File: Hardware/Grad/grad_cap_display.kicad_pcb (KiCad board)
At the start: 4 copper layers, 76.5 x 76.5 mm, 62 parts, among them J101 6-Pos 2.54mm Header, J1101 JST-PH SPI, J1102 JST-PH UART/I2C, J1103 JST-PH A#, J1104 Micro_SD_Card, J201 Amphenol 40-Pin FPC, J202 01x30 Pads, J203 01x30 Pads, J204 01x30 Pads, J205 01x30 Pads, J3 2x8 2.54mm IDC Header, U1101 TC7MBL3126CFT, U1102 AZ1117-5.0, U1103 THVD1400D, U1104 QTPy SAMD21, U201 LM66200DRLR, U202 TLV75733PDRV, U203 SN74LVC1G139, U204 ESP32-S3-WROOM-1-N8R8, U205 TC7MBL3126CFT, U206 AP3019AKTTR, U207 W25Q128JVP, U208 THVD1400D

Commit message: More routing progress
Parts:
- removed C1101, C1104, C1105: 100nF, Capacitor_SMD:C_0402_1005Metric
- removed C1102, C1103, C1106: 22uF, Capacitor_SMD:C_0603_1608Metric
- removed C201, C203: 1uF, New_Library:Worthington_C_0603
- removed C202, C204, C206, C215: 22uF, New_Library:Worthington_C_0603
- removed C205, C207, C208, C209, C210, C211, C213, C214, C216: 100nF, New_Library:Worthington_C_0402
- removed C212: 22uF, New_Library:Worthington_D_0603
- removed D1101, D1102: LED_Small, New_Library:Worthington_LED_0603
- removed D201, D202, D203, D204, D205: RED, New_Library:Worthington_LED_0603
- removed J1101: JST-PH SPI, Connector_JST:JST_PH_S5B-PH-K_1x05_P2.00mm_Horizontal
- removed J1102: JST-PH UART/I2C, Connector_JST:JST_PH_S6B-PH-K_1x06_P2.00mm_Horizontal
- removed J1103: JST-PH A#, Connector_JST:JST_PH_S6B-PH-K_1x06_P2.00mm_Horizontal
- removed L201: 22uH, New_Library:CDRH5D28
- removed R1101: 1k, New_Library:Worthington_R_0402
- removed R1102, R201: 430, New_Library:Worthington_R_0402
- removed R202: 10, Resistor_SMD:R_1210_3225Metric
- removed R203: 120, New_Library:Worthington_R_0402
- removed RN1101: 47k, New_Library:RESCAXE80P320X160X70-8N
- removed RN201: 10k, New_Library:RESCAXE80P320X160X70-8N
- removed RN202: 430, New_Library:RESCAXE80P320X160X70-8N
- removed U1101, U205: TC7MBL3126CFT, Package_SO:TSSOP-14_4.4x5mm_P0.65mm
- removed U1102: AZ1117-5.0, Package_TO_SOT_SMD:SOT-223-3_TabPin2
- removed U1103, U208: THVD1400D, Package_SO:SOIC-8_3.9x4.9mm_P1.27mm
- removed U201: LM66200DRLR, Package_TO_SOT_SMD:SOT-583-8
- removed U202: TLV75733PDRV, Package_SON:WSON-6-1EP_2x2mm_P0.65mm_EP1x1.6mm
- removed U203: SN74LVC1G139, Package_SO:VSSOP-8_2.3x2mm_P0.5mm
- removed U206: AP3019AKTTR, Package_TO_SOT_SMD:TSOT-23-6
- removed U207: W25Q128JVP, Package_SON:WSON-8-1EP_6x5mm_P1.27mm_EP3.4x4.3mm
- added C101: 22uF, New_Library:Worthington_C_0603, F.Cu at (61.2, 9.75)
- added C102: 22uF, New_Library:Worthington_C_0603, F.Cu at (4.15, 5.95)
- added C103: 22uF, New_Library:Worthington_C_0603, F.Cu at (9.65, 11.8)
- added C104: 22uF, New_Library:Worthington_C_0603, F.Cu at (16.4, 11.7)
- added C105: 100nF, New_Library:Worthington_C_0402, F.Cu at (18.1, 12.0)
- added C106: 100nF, New_Library:Worthington_C_0402, F.Cu at (14.8, 12.0)
- added C107: 22uF, New_Library:Worthington_C_0603, F.Cu at (22.8, 11.6)
- added C108: 100nF, New_Library:Worthington_C_0402, F.Cu at (61.2, 13.1)
- added C109: 100nF, New_Library:Worthington_C_0402, F.Cu at (25.8, 11.2)
- added C110: 100nF, New_Library:Worthington_C_0402, F.Cu at (24.4, 11.2)
- added C111: 100nF, New_Library:Worthington_C_0402, F.Cu at (56.4, 6.85)
- added C112: 100nF, New_Library:Worthington_C_0402, F.Cu at (58.3, 23.0)
- added C113: 22uF, New_Library:Worthington_C_0603, F.Cu at (68.5, 68.7)
- added C114: 100nF, New_Library:Worthington_C_0402, F.Cu at (52.1, 57.0)
- added C115: 100nF, New_Library:Worthington_C_0402, F.Cu at (67.1, 68.4)
- added C116: 22uF, New_Library:Worthington_C_0603, F.Cu at (52.4, 58.5)
- added C217: 100nF, Capacitor_SMD:C_0402_1005Metric, F.Cu at (29.3, 39.7)
- added C218: 22uF, Capacitor_SMD:C_0603_1608Metric, F.Cu at (7.50, 23.8)
- added C219: 22uF, Capacitor_SMD:C_0603_1608Metric, F.Cu at (10.4, 24.6)
- added C220: 100nF, Capacitor_SMD:C_0402_1005Metric, F.Cu at (10.2, 26.0)
- added C221: 100nF, Capacitor_SMD:C_0402_1005Metric, F.Cu at (56.0, 41.5)
- added C222: 22uF, Capacitor_SMD:C_0603_1608Metric, F.Cu at (54.6, 42.0)
- added C223: 22uF, Capacitor_SMD:C_0603_1608Metric, F.Cu at (17.3, 26.4)
- added C401: 100nF, New_Library:Worthington_C_0402, F.Cu at (53.3, 14.2)
- added C402: 100nF, Capacitor_SMD:C_0402_1005Metric, F.Cu at (37.1, 45.0)
- added D101: RED, New_Library:Worthington_LED_0603, F.Cu at (19.6, 11.6)
- added D102: RED, New_Library:Worthington_LED_0603, F.Cu at (47.6, 80.8)
- added D103: RED, New_Library:Worthington_LED_0603, F.Cu at (47.6, 83.3)
- added D104: RED, New_Library:Worthington_LED_0603, F.Cu at (47.6, 85.8)
- added D105: RED, New_Library:Worthington_LED_0603, F.Cu at (47.6, 88.3)
- added D206: RED, New_Library:Worthington_LED_0603, F.Cu at (12.8, 19.8)
- added D207: RED, New_Library:Worthington_LED_0603, F.Cu at (65.4, 47.5)
- added D208: RED, New_Library:Worthington_LED_0603, F.Cu at (17.3, 24.7)
- added J102: 6-Pos 2.54mm Header, Connector_PinHeader_2.54mm:PinHeader_1x06_P2.54mm_Vertical_SMD_Pin1Left, F.Cu at (65.3, 6.50)
- added J207: SPI TestPoint, Connector_PinHeader_2.54mm:PinHeader_1x06_P2.54mm_Vertical_SMD_Pin1Right, F.Cu at (15.0, 54.1)
- added J208: RS485 TestPoint, Connector_PinHeader_2.54mm:PinHeader_1x05_P2.54mm_Vertical_SMD_Pin1Right, F.Cu at (13.8, 63.8)
- added J209: Extra TestPoint, Connector_PinHeader_2.54mm:PinHeader_1x05_P2.54mm_Vertical_SMD_Pin1Right, F.Cu at (13.8, 68.6)
- added J211: Push Button Header, Connector_PinHeader_2.54mm:PinHeader_1x06_P2.54mm_Vertical_SMD_Pin1Right, F.Cu at (15.0, 58.9)
- added J405: LCD Power TestPoint, Connector_PinHeader_2.54mm:PinHeader_1x02_P2.54mm_Vertical_SMD_Pin1Right, F.Cu at (58.1, 70.4)
- added L101: 22uH, New_Library:CDRH5D28, F.Cu at (62.9, 65.8)
- added R101: 430, New_Library:Worthington_R_0402, F.Cu at (21.2, 11.2)
- added R102: 10, Resistor_SMD:R_1210_3225Metric, F.Cu at (57.6, 58.2)
- added R103: 120, New_Library:Worthington_R_0402, F.Cu at (58.1, 24.9)
- added R104: 10, Resistor_SMD:R_1210_3225Metric, F.Cu at (56.7, 50.7)
- added R105: 10, Resistor_SMD:R_1210_3225Metric, F.Cu at (53.5, 50.7)
- added R207: 1k, New_Library:Worthington_R_0402, F.Cu at (10.2, 23.1)
- added R208: 1k, New_Library:Worthington_R_0402, F.Cu at (62.2, 47.5)
- added R209: 430, New_Library:Worthington_R_0402, F.Cu at (17.6, 23.3)
- added R401: 100, New_Library:Worthington_R_0402, F.Cu at (48.9, 45.1)
- added R402: 100, New_Library:Worthington_R_0402, F.Cu at (46.9, 44.4)
- added R403: 100, New_Library:Worthington_R_0402, F.Cu at (48.9, 43.9)
- added RN101: 10k, New_Library:RESCAXE80P320X160X70-8N, F.Cu at (91.7, 43.8)
- added RN102: 430, New_Library:RESCAXE80P320X160X70-8N, F.Cu at (88.0, 40.4)
- added RN203: 47k, New_Library:RESCAXE80P320X160X70-8N, F.Cu at (63.0, 50.1)
- added RN204: 10k, New_Library:RESCAXE80P320X160X70-8N, F.Cu at (4.99, 58.2)
- added U101: LM66200DRLR, Package_TO_SOT_SMD:SOT-583-8, F.Cu at (7.45, 13.8)
- added U102: TLV75733PDRV, Package_SON:WSON-6-1EP_2x2mm_P0.65mm_EP1x1.6mm, F.Cu at (11.9, 12.9)
- added U103: SN74LVC1G139, Package_SO:VSSOP-8_2.3x2mm_P0.5mm, F.Cu at (59.2, 13.0)
- added U105: TC7MBL3126CFT, Package_SO:TSSOP-14_4.4x5mm_P0.65mm, F.Cu at (53.3, 10.7)
- added U106: AP3019AKTTR, Package_TO_SOT_SMD:TSOT-23-6, F.Cu at (57.4, 65.2)
- added U107: THVD1400D, Package_SO:SOIC-8_3.9x4.9mm_P1.27mm, F.Cu at (53.6, 24.9)
- added U108: W25Q128JVP, Package_SON:WSON-8-1EP_6x5mm_P1.27mm_EP3.4x4.3mm, F.Cu at (53.1, 17.7)
- added U209: TC7MBL3126CFT, Package_SO:TSSOP-14_4.4x5mm_P0.65mm, F.Cu at (42.3, 45.0)
- added U210: THVD1400D, Package_SO:SOIC-8_3.9x4.9mm_P1.27mm, F.Cu at (31.4, 44.1)
- added U211: AZ1117-5.0, Package_TO_SOT_SMD:SOT-89-3, F.Cu at (9.15, 20.0)
- J101: value 6-Pos 2.54mm Header -> Power In; footprint Connector_PinHeader_2.54mm:PinHeader_1x06_P2.54mm_Vertical_SMD_Pin1Left -> Connector_JST:JST_PH_S2B-PH-K_1x02_P2.00mm_Horizontal
- moved J402 756.6 mm to (75.1, 0.00), turned to -90 degrees
- moved R204 753.1 mm to (31.4, 39.7), turned to 180 degrees
- moved J103 728.5 mm to (44.5, 35.4)
- moved U212 727.9 mm to (16.8, 38.2)
- moved U104 726.6 mm to (38.3, 12.9)
- moved J104 726.2 mm to (38.3, 52.8)
- moved J210 726.2 mm to (65.7, 38.2)
- moved J401 726.2 mm to (0.04, 1.49)
- moved J404 726.2 mm to (76.5, 75.1)
- moved J101 702.7 mm to (6.95, 7.70), turned to 90 degrees
- moved J403 702.2 mm to (1.49, 76.6), turned to 90 degrees
- renumbered J3 to J103, J201 to J104, J1104 to J210, J202 to J401, J203 to J402, J205 to J403, J204 to J404, U204 to U104, U1104 to U212
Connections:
- net /ESP32 1/+3V3 renamed /+3V3
- net /ESP32 1/LCD_RGB_DB0 renamed /LCD_RGB_DB0
- net /ESP32 1/LCD_RGB_DB1 renamed /LCD_RGB_DB1
- net /ESP32 1/LCD_RGB_DB10 renamed /LCD_RGB_DB10
- net /ESP32 1/LCD_RGB_DB11 renamed /LCD_RGB_DB11
- net /ESP32 1/LCD_RGB_DB12 renamed /LCD_RGB_DB12
- net /ESP32 1/LCD_RGB_DB13 renamed /LCD_RGB_DB13
- net /ESP32 1/LCD_RGB_DB14 renamed /LCD_RGB_DB14
- net /ESP32 1/LCD_RGB_DB15 renamed /LCD_RGB_DB15
- net /ESP32 1/LCD_RGB_DB16 renamed /LCD_RGB_DB16
- net /ESP32 1/LCD_RGB_DB17 renamed /LCD_RGB_DB17
- net /ESP32 1/LCD_RGB_DB2 renamed /LCD_RGB_DB2
- net /ESP32 1/LCD_RGB_DB3 renamed /LCD_RGB_DB3
- net /ESP32 1/LCD_RGB_DB4 renamed /LCD_RGB_DB4
- net /ESP32 1/LCD_RGB_DB5 renamed /LCD_RGB_DB5
- net /ESP32 1/LCD_RGB_DB6 renamed /LCD_RGB_DB6
- net /ESP32 1/LCD_RGB_DB7 renamed /LCD_RGB_DB7
- net /ESP32 1/LCD_RGB_DB8 renamed /LCD_RGB_DB8
- net /ESP32 1/LCD_RGB_DB9 renamed /LCD_RGB_DB9
- net /ESP32 1/LCD_RGB_PCLK renamed /LCD_RGB_PCLK
- net /ESP32 1/LCD_RGB_VSYNC renamed /LCD_RGB_VSYNC
- net /ESP32 1/RS485_A renamed /RS485_A
- net /ESP32 1/RS485_B renamed /RS485_B
- net /ESP32 1/SAMD21_3V3 renamed /SAMD21_3V3
- net /ESP32 1/SPI_MISO_µSD renamed /µSD_SPI_MISO
- net /ESP32 1/SPI_MOSI_µSD renamed /µSD_SPI_MOSI
- net /ESP32 1/SPI_SCK_µSD renamed /µSD_SPI_SCK
- net /ESP32 1/STRAP_GPIO3 renamed /STRAP_GPIO3
- J101 pad 1: /ESP32 1/ESP_PROG_PWR -> /BATT_IN
- J101 pad 2: /ESP32 1/ESP_PROG_EN -> GND
- J103 pad 1: /ESP32 1/BATT_IN -> GND
- J103 pad 10: /ESP32 1/FRAME_SYNC_IN -> /FRAME_SYNC
- J103 pad 12: /ESP32 1/BATT_IN -> GND
- J103 pad 3: /ESP32 1/SPI_CS_µSD -> /µSD_SPI_CS
- J103 pad 8: /ESP32 1/BACKLIGHT_PWM_IN -> /BACKLIGHT_PWM
- J104 pad 26: /ESP32 1/LCD_RGB_HSYNC -> /LCD_RGB_HSYNC
- J104 pad 28: /ESP32 1/LCD_RGB_DE -> /LCD_RGB_DE
- J104 pad 30: /ESP32 1/SPI_CS_LCD -> /ESP_CS_LCD
- J104 pad 31: /ESP32 1/SPI_SCK -> /ESP_SCK_T
- J104 pad 32: /ESP32 1/SPI_MOSI -> /ESP_MOSI_T
- J210 pad 2: /ESP32 1/SPI_CS_µSD -> /µSD_SPI_CS
- J210 pad CD: unconnected-(J1104-CHIP_DETECT-PadCD) -> Net-(J210-CHIP_DETECT)
- J401 pad 25: GND -> /BATT_IN
- J401 pad 26: GND -> /BATT_IN
- J401 pad 5: GND -> /BATT_IN
- J401 pad 6: GND -> /BATT_IN
- J402 pad 25: GND -> /BATT_IN
- J402 pad 26: GND -> /BATT_IN
- J402 pad 5: GND -> /BATT_IN
- J402 pad 6: GND -> /BATT_IN
- J403 pad 25: GND -> /BATT_IN
- J403 pad 26: GND -> /BATT_IN
- J403 pad 5: GND -> /BATT_IN
- J403 pad 6: GND -> /BATT_IN
- J404 pad 23: GND -> Net-(J404-Pin_1)
- J404 pad 24: GND -> Net-(J404-Pin_1)
- J404 pad 25: GND -> /BATT_IN
- J404 pad 26: GND -> /BATT_IN
- J404 pad 3: GND -> Net-(J404-Pin_1)
- J404 pad 4: GND -> Net-(J404-Pin_1)
- J404 pad 5: GND -> /BATT_IN
- J404 pad 6: GND -> /BATT_IN
- J404 pad 7: GND -> Net-(J404-Pin_1)
- J404 pad 8: GND -> Net-(J404-Pin_1)
- U104 pad 12: /ESP32 1/SPI_MOSI -> /ESP_MOSI
- U104 pad 16: /ESP32 1/SPI_CS1 -> /ESP_CS0
- U104 pad 17: /ESP32 1/SPI_SCK -> /ESP_SCK
- U104 pad 18: /ESP32 1/SPI_CS0 -> /ESP_CS1
- U104 pad 19: /ESP32 1/UART-RS485_TX -> /UART-RS485_TX
- U104 pad 20: /ESP32 1/UART-RS485_RX -> /UART-RS485_RX
- U104 pad 23: /ESP32 1/UART_RS485_DE -> /UART_RS485_DE
- U104 pad 26: /ESP32 1/SPI_MISO -> /ESP_MISO
- U104 pad 27: /ESP32 1/ESP_PROG_IO0 -> /ESP_PROG_IO0
- U104 pad 3: /ESP32 1/ESP_PROG_EN -> /ESP_PROG_EN
- U104 pad 32: /ESP32 1/LCD_RGB_HSYNC -> /LCD_RGB_DE
- U104 pad 34: /ESP32 1/LCD_RGB_DE -> /LCD_RGB_HSYNC
- U104 pad 36: /ESP32 1/ESP_PROG_RXD0 -> /ESP_PROG_RXD0
- U104 pad 37: /ESP32 1/ESP_PROG_TXD0 -> /ESP_PROG_TXD0
- U104 pad 39: /ESP32 1/FRAME_SYNC -> /FRAME_SYNC
- U212 pad 1: /ESP32 1/SPI_µSD_BUS_CONNECT -> /SAMD_µSD_BUS_CONNECT
- U212 pad 10: /ESP32 1/SAMD_MISO -> /SAMD_MISO
- U212 pad 11: /ESP32 1/SAMD_MOSI -> /SAMD_MOSI
- U212 pad 14: /ESP32 1/SAMD21_5V -> /SAMD21_5V
- U212 pad 2: /ESP32 1/SPI_CS_µSD -> /SAMD_CS_µSD
- U212 pad 3: /ESP32 1/FRAME_SYNC -> /FRAME_SYNC
- U212 pad 4: /ESP32 1/UART_RS485_DE -> /BUTTON_SENSE
- U212 pad 5: /ESP32 1/SAMD_SDA -> /SAMD_UART-RS485_DE
- U212 pad 6: /ESP32 1/BACKLIGHT_PWM -> /BACKLIGHT_PWM
- U212 pad 7: /ESP32 1/UART-RS485_TX -> /SAMD_UART-RS485_TX
- U212 pad 8: /ESP32 1/UART-RS485_RX -> /SAMD_UART-RS485_RX
- U212 pad 9: /ESP32 1/SAMD_SCK -> /SAMD_SCK
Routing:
- net /BATT_IN: track 0.00 -> 108.4 mm, vias 0 -> 19
- net /ESP_MOSI: track 0.00 -> 86.6 mm, vias 0 -> 2
- net /ESP_SCK: track 0.00 -> 76.2 mm, vias 0 -> 2
- net /ESP_PROG_PWR: track 0.00 -> 60.4 mm, vias 0 -> 2
- net /SAMD_µSD_BUS_CONNECT: track 0.00 -> 59.9 mm, vias 0 -> 2
- net /RS485_B: track 0.00 -> 56.0 mm
- net /RS485_A: track 0.00 -> 56.0 mm
- net /LCD_RGB_DB0: track 0.00 -> 51.6 mm, vias 0 -> 2
- net /LCD_RGB_DB1: track 0.00 -> 49.5 mm, vias 0 -> 2
- net /LCD_RGB_DB13: track 0.00 -> 48.5 mm, vias 0 -> 2
- net /LCD_RGB_DB2: track 0.00 -> 47.1 mm, vias 0 -> 2
- net /LCD_RGB_DB3: track 0.00 -> 46.7 mm, vias 0 -> 2
- net /ESP_PROG_IO0: track 0.00 -> 45.0 mm, vias 0 -> 2
- net /+3V3: track 0.00 -> 45.0 mm, vias 0 -> 19
- net /LCD_RGB_DB4: track 0.00 -> 44.8 mm, vias 0 -> 2
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- added copper zone on F.Cu, net /+3V3
- added copper zone on F.Cu, net /BATT_IN
- added copper zone on In2.Cu, net /BATT_IN
- added copper zone on F.Cu, net /PWR_IN
- added copper zone on F.Cu, net /SAMD21_3V3
- added copper zone on In2.Cu, net /SAMD21_3V3
- added copper zone on F.Cu, net Net-(J104-LEDA)
- added copper zone on F.Cu, net Net-(U106-FB)
- added copper zone on F.Cu, net Net-(U106-SW)
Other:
- outline, holes or cut-outs redrawn

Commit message: Small tweaks
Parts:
- moved J101 1.28 mm to (8.23, 7.69)
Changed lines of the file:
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@@
 	(footprint "Connector_JST:JST_PH_S2B-PH-K_1x02_P2.00mm_Horizontal"
 		(layer "F.Cu")
-		(at 6.95 7.7 90)
+		(at 8.230076 7.692469 90)
 		(descr "JST PH series connector, S2B-PH-K (http://www.jst-mfg.com/product/pdf/eng/ePH.pdf), generated with kicad-footprint-generator")
 		(tags "connector JST PH horizontal")
@@
 		(polygon
 			(pts
-				(xy 0 3.75) (xy 0 21.25) (xy 6.05 21.25) (xy 6.05 13.5) (xy 6.05 13.25) (xy 6.05 12.45) (xy 8.35 10.15)
-				(xy 8.35 3.75)
+				(xy 0 3.75) (xy 0 21.25) (xy 6.05 21.25) (xy 6.05 13.5) (xy 6.05 13.25) (xy 6.05 12.45) (xy 10.64 7.86)
+				(xy 10.64 3.75)
 			)
 		)

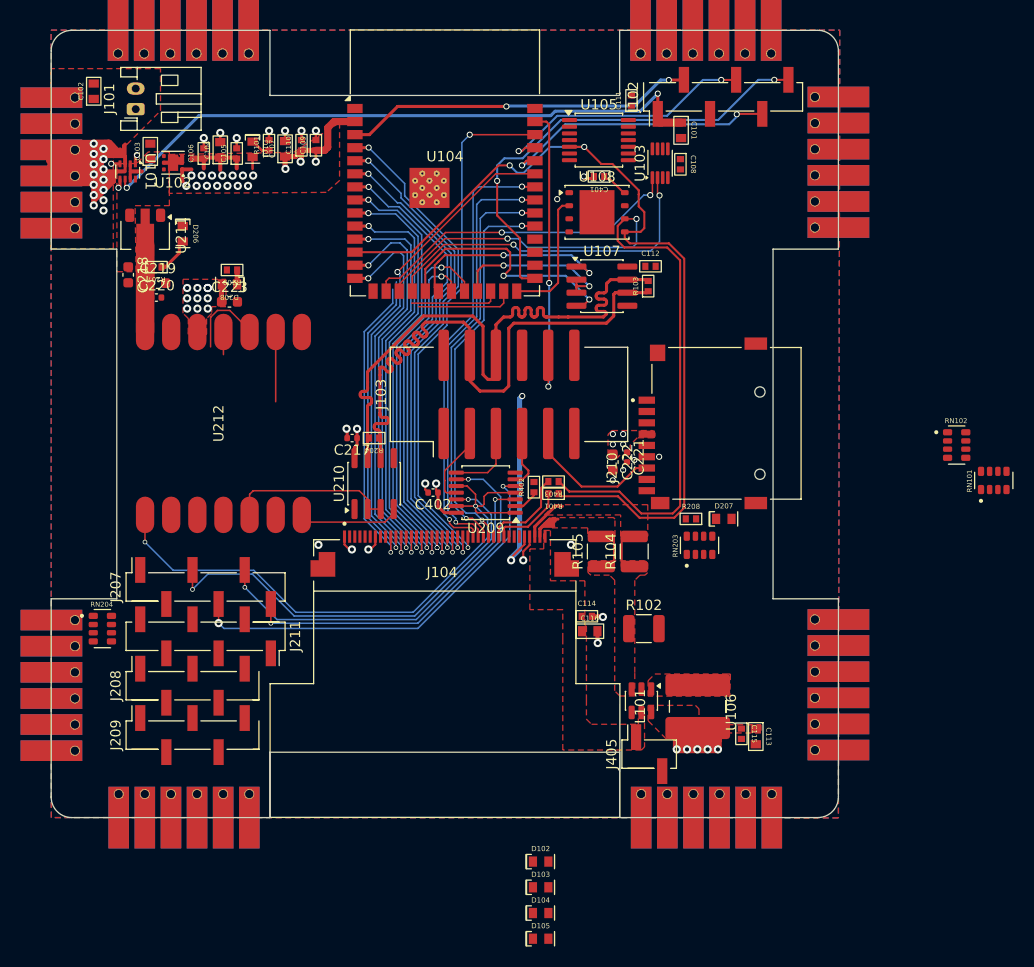
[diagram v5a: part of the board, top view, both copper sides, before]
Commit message: Rev A gerbers generated, sent to fab
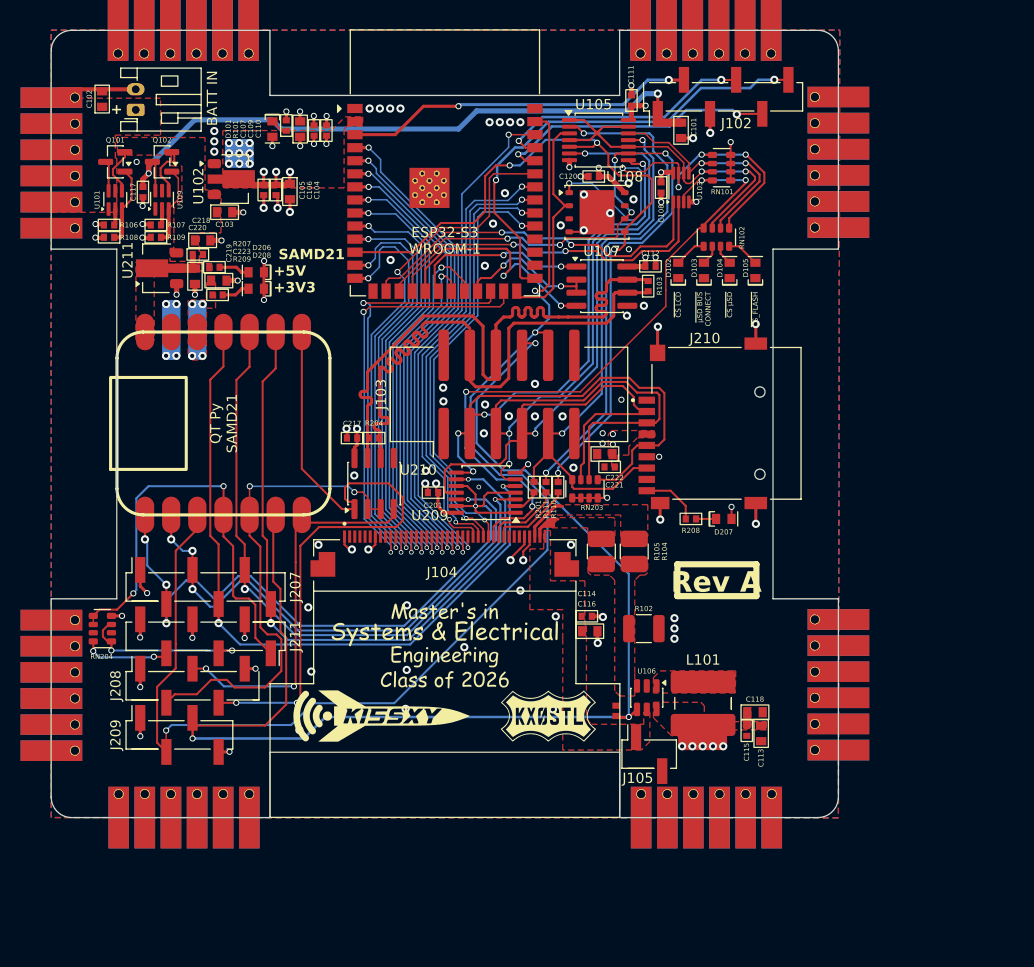
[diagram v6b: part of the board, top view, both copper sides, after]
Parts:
- added C117: 100nF, New_Library:Worthington_C_0402, F.Cu at (8.93, 15.8)
- added C118: 22uF, New_Library:Worthington_C_0603, F.Cu at (68.4, 66.3)
- added C119: ~, New_Library:Worthington_C_0402, F.Cu at (54.9, 66.2)
- added G***: LOGO, New_Library:Masters_Text, F.Cu at (38.3, 62.7)
- added Q101: DMP2045U, Package_TO_SOT_SMD:SOT-23, F.Cu at (6.24, 12.8)
- added Q102: DMP2045U, Package_TO_SOT_SMD:SOT-23, F.Cu at (10.8, 12.8)
- added R106: 100k, New_Library:Worthington_R_0402, F.Cu at (5.64, 19.0)
- added R107: 100k, New_Library:Worthington_R_0402, F.Cu at (10.2, 19.0)
- added R108: 1M, New_Library:Worthington_R_0402, F.Cu at (5.64, 20.2)
- added R109: 1M, New_Library:Worthington_R_0402, F.Cu at (10.2, 20.2)
- added U109: DZDH0401DW, Package_TO_SOT_SMD:SOT-363_SC-70-6, F.Cu at (10.8, 16.5)
- C201: renamed from C402; footprint Capacitor_SMD:C_0402_1005Metric -> New_Library:Worthington_C_0402
- C217, C220, C221: footprint Capacitor_SMD:C_0402_1005Metric -> New_Library:Worthington_C_0402
- C218, C219, C222, C223: footprint Capacitor_SMD:C_0603_1608Metric -> New_Library:Worthington_C_0603
- J209: footprint Connector_PinHeader_2.54mm:PinHeader_1x05_P2.54mm_Vertical_SMD_Pin1Right -> Connector_PinHeader_2.54mm:PinHeader_1x04_P2.54mm_Vertical_SMD_Pin1Right
- U101: value LM66200DRLR -> DZDH0401DW; footprint Package_TO_SOT_SMD:SOT-583-8 -> Package_TO_SOT_SMD:SOT-363_SC-70-6
- U102: value TLV75733PDRV -> AZ1117-5.0; footprint Package_SON:WSON-6-1EP_2x2mm_P0.65mm_EP1x1.6mm -> Package_TO_SOT_SMD:SOT-89-3
- moved D105 68.2 mm to (68.5, 23.4), turned to 90 degrees
- moved D104 65.1 mm to (66.0, 23.4), turned to 90 degrees
- moved D103 62.0 mm to (63.5, 23.4), turned to 90 degrees
- moved D102 59.0 mm to (61.0, 23.4), turned to 90 degrees
- moved RN101 40.3 mm to (65.2, 13.4), turned to 180 degrees
- moved RN102 30.9 mm to (64.7, 20.1), turned to 90 degrees
- moved RN203 12.4 mm to (51.9, 44.6)
- moved C103 9.33 mm to (16.9, 17.7), turned to 0 degrees
- moved D206 8.07 mm to (20.0, 23.6), turned to 180 degrees
- moved C218 7.97 mm to (14.7, 20.5), turned to 0 degrees
- moved C104 7.89 mm to (23.2, 15.7), turned to -90 degrees
- moved C106 7.87 mm to (21.9, 15.6), turned to -90 degrees
- moved U102 6.17 mm to (17.8, 14.5), turned to 0 degrees
- moved C220 5.81 mm to (14.3, 21.8)
- moved R207 5.64 mm to (15.9, 23.1)
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- renumbered C401 to C120, J405 to J105, R401 to R110, R403 to R111, R402 to R201
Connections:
- D208 pad 1: Net-(D208-K) -> GND
- D208 pad 2: /SAMD21_3V3 -> Net-(D208-A)
- J103 pad 3: /µSD_SPI_CS -> /µSD_SPI_SCK
- J103 pad 5: /µSD_SPI_SCK -> /µSD_SPI_MOSI
- J103 pad 7: /µSD_SPI_MOSI -> /µSD_SPI_CS
- J104 pad 38: Net-(U106-FB) -> Net-(J104-LEDK-Pad38)
- J104 pad 39: Net-(U106-FB) -> Net-(J104-LEDK-Pad39)
- J209 pad 2: unconnected-(J209-Pin_2-Pad2) -> /FRAME_SYNC
- J209 pad 3: /FRAME_SYNC -> /BACKLIGHT_PWM
- J209 pad 4: /BACKLIGHT_PWM -> GND
- J404 pad 23: Net-(J404-Pin_1) -> GND
- J404 pad 24: Net-(J404-Pin_1) -> GND
- J404 pad 3: Net-(J404-Pin_1) -> GND
- J404 pad 4: Net-(J404-Pin_1) -> GND
- J404 pad 7: Net-(J404-Pin_1) -> GND
- J404 pad 8: Net-(J404-Pin_1) -> GND
- R104 pad 2: Net-(U106-FB) -> Net-(J104-LEDK-Pad38)
- R105 pad 2: Net-(U106-FB) -> Net-(J104-LEDK-Pad39)
- R209 pad 1: Net-(D208-K) -> Net-(D208-A)
- R209 pad 2: GND -> /SAMD21_3V3
- RN101 pad 5: /ESP_µSD_BUS_CONNECT -> /ESP_CS_FLASH
- RN101 pad 7: /ESP_CS_FLASH -> /ESP_µSD_BUS_CONNECT
- RN102 pad 5: /ESP_CS_LCD -> /ESP_CS_FLASH
- RN102 pad 6: /ESP_CS_FLASH -> /ESP_CS_µSD
- RN102 pad 7: /ESP_CS_µSD -> /ESP_µSD_BUS_CONNECT
- RN102 pad 8: /ESP_µSD_BUS_CONNECT -> /ESP_CS_LCD
- RN203 pad 5: /µSD_SPI_CS -> /µSD_SPI_SCK
- RN203 pad 6: /µSD_SPI_MISO -> /µSD_SPI_MOSI
- RN203 pad 7: /µSD_SPI_MOSI -> /µSD_SPI_CS
- RN203 pad 8: /µSD_SPI_SCK -> /µSD_SPI_MISO
- RN204 pad 3: Net-(J211-Pin_5) -> unconnected-(RN204-Pad3)
- RN204 pad 4: unconnected-(RN204-Pad4) -> Net-(J211-Pin_5)
- RN204 pad 5: unconnected-(RN204-Pad5) -> Net-(J211-Pin_3)
- RN204 pad 6: Net-(J211-Pin_3) -> unconnected-(RN204-Pad6)
- U101 pad 1: GND -> unconnected-(U101-NC-Pad1)
- U101 pad 2: /PWR_IN -> Net-(U101-REF)
- U101 pad 3: /BATT_IN -> Net-(Q101-G)
- U101 pad 4: GND -> /PWR_IN
- U101 pad 5: GND -> unconnected-(U101-NC-Pad5)
- U101 pad 6: /ESP_PROG_PWR -> /BATT_IN
- U102 pad 1: /+3V3 -> GND
- U102 pad 2: GND -> /+3V3
- U102 pad 3: GND -> /PWR_IN
- U103 pad 3: /ESP_µSD_BUS_CONNECT -> /ESP_CS_LCD
- U103 pad 6: /ESP_CS_FLASH -> /ESP_µSD_BUS_CONNECT
- U103 pad 7: /ESP_CS_LCD -> /ESP_CS_FLASH
- U108 pad 9: unconnected-(U108-EP-Pad9) -> GND
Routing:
- net /BACKLIGHT_PWM: track 0.00 -> 124.7 mm, vias 0 -> 3
- net /FRAME_SYNC: track 30.1 -> 125.7 mm, vias 2 -> 3
- net /µSD_SPI_MOSI: track 5.68 -> 85.0 mm, vias 0 -> 3
- net /BATT_IN: track 108.4 -> 29.2 mm, vias 19 -> 5
- net /µSD_SPI_SCK: track 7.19 -> 82.4 mm, vias 0 -> 4
- net /µSD_SPI_CS: track 7.80 -> 79.4 mm, vias 0 -> 2
- net /ESP_CS_LCD: track 0.00 -> 68.8 mm, vias 0 -> 4
- net GND: track 22.7 -> 90.4 mm, vias 25 -> 107
- net /SAMD_UART-RS485_RX: track 0.00 -> 65.4 mm, vias 0 -> 2
- net /µSD_SPI_MISO: track 13.6 -> 65.0 mm, vias 0 -> 2
- net /BUTTON_SENSE: track 0.00 -> 42.9 mm, vias 0 -> 2
- net /ESP_CS_FLASH: track 0.00 -> 42.8 mm, vias 0 -> 5
- net /ESP_µSD_BUS_CONNECT: track 0.00 -> 38.2 mm, vias 0 -> 2
- net /SAMD_UART-RS485_DE: track 16.2 -> 47.2 mm, vias 0 -> 2
- net /SAMD_UART-RS485_TX: track 9.99 -> 37.8 mm, vias 0 -> 2
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- added copper zone on F.Cu, net /SAMD21_5V
- added copper zone on F.Cu, net Net-(J104-LEDK-Pad38)
- added copper zone on F.Cu, net Net-(J104-LEDK-Pad39)
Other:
- board text added: "+"
- board text added: "BATT IN"
- board text added: "ESP32-S3 WROOM-1"
- board text added: "QT Py SAMD21"
- board text added: "Rev A"
- board text added: "SAMD21 +5V +3V3"
- board text added: "~{CS LCD}"
- board text added: "~{CS µSD}"
- board text added: "~{CS_FLASH}"
- board text added: "~{µSD BUS} CONNECT"
